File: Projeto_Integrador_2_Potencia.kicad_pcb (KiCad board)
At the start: 2 copper layers, 114 x 59.4 mm, 17 parts, among them J10 Borne_CMD_Interface, J2 Vi 24V, J3 Vo 48V, J4 INA219_01x02_Socket_3.5mm, J5 INA219_01x06_Socket_2.55mm, J7 Display_01x04_Socket, J9 PWM_Connector, Q1 IRF740, U1 ESP32-DEVKIT-V1

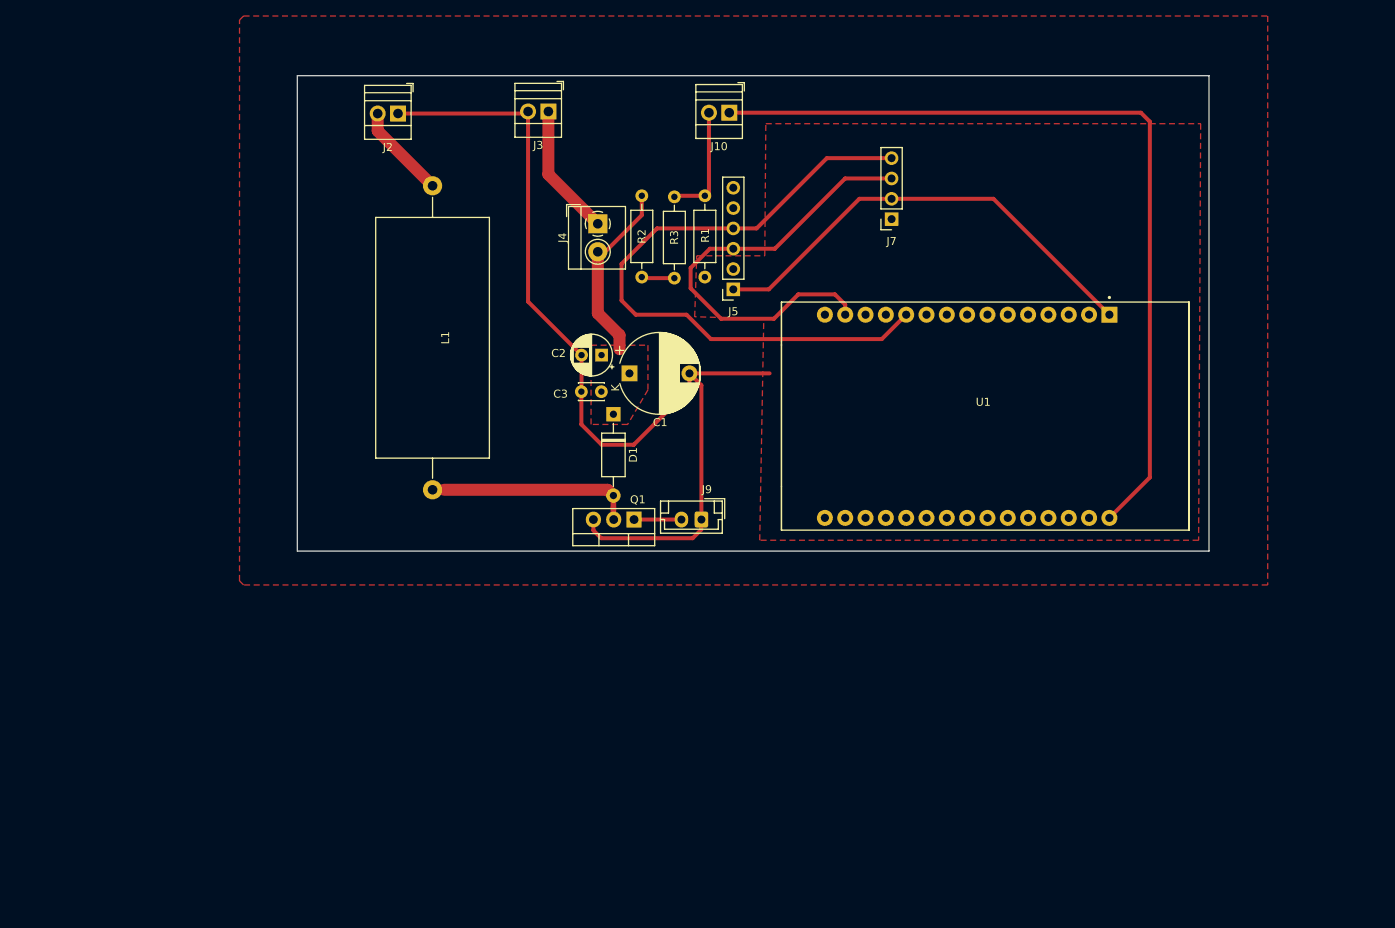
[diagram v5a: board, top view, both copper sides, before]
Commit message: Adição de recuo nas bordas do layout
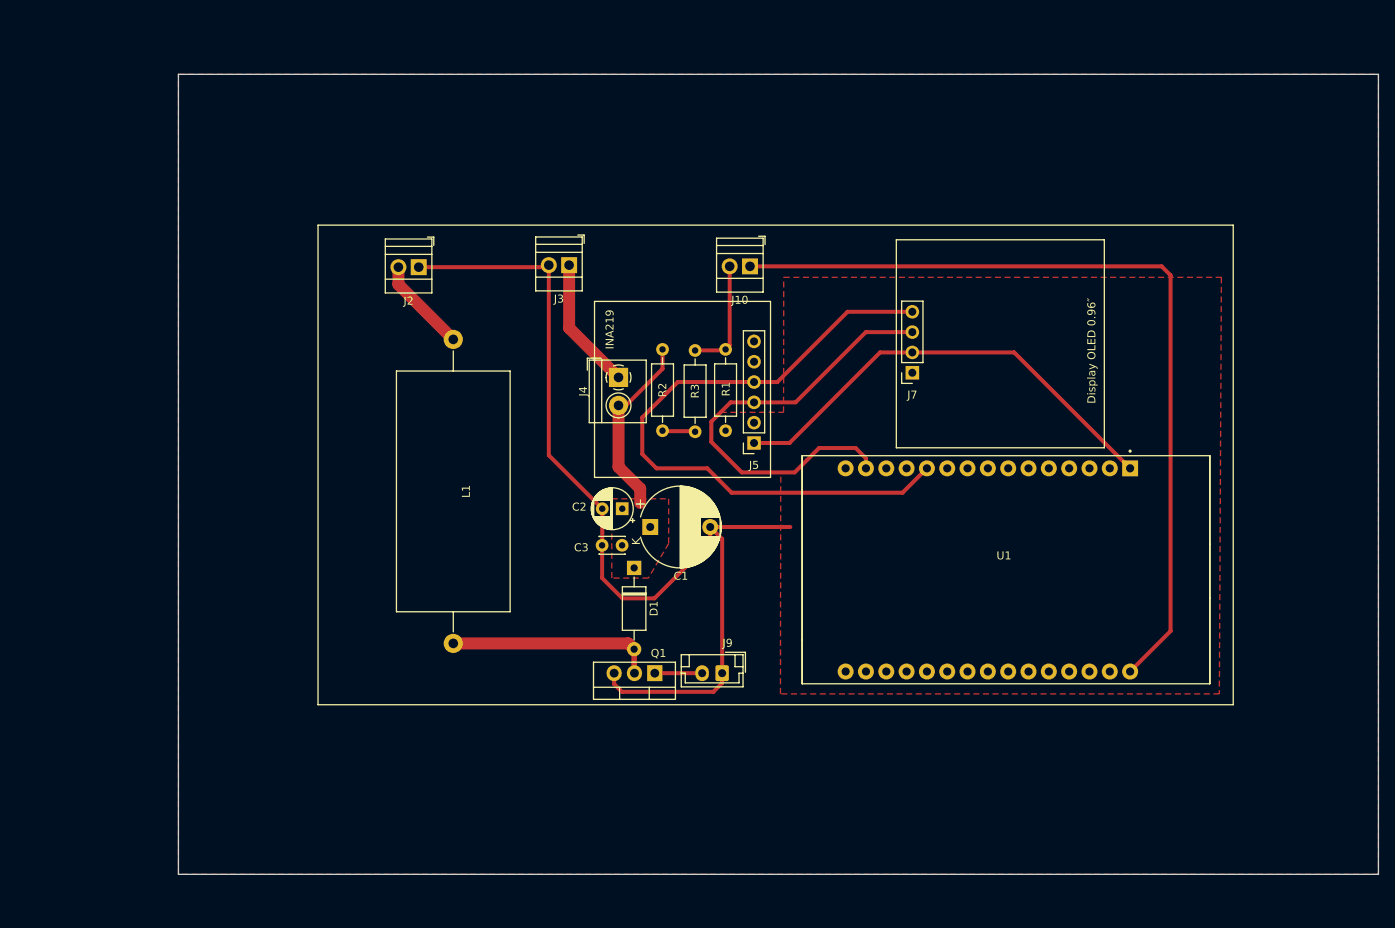
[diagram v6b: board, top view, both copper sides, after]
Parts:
- moved J10 19.4 mm to (135.9, 69.9)
- moved J2 19.4 mm to (94.5, 70.0)
- moved R1 19.4 mm to (132.9, 80.3)
- moved D1 19.4 mm to (121.5, 107.6)
- moved J4 19.4 mm to (119.5, 83.8)
- moved L1 19.4 mm to (98.9, 79.0)
- moved R2 19.4 mm to (125.0, 80.3)
- moved R3 19.4 mm to (129.1, 90.6)
- moved J3 19.4 mm to (113.3, 69.8)
- moved J7 19.4 mm to (156.2, 83.2)
- moved C3 19.4 mm to (120.0, 104.8)
- moved J5 19.4 mm to (136.4, 92.0)
- moved Q1 19.4 mm to (124.0, 120.8)
- moved C1 19.4 mm to (123.5, 102.5)
- moved C2 19.4 mm to (120.0, 100.2)
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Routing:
- net Net-(D1-A): track 26.0 -> 27.4 mm
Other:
- board size 114 x 59.4 mm -> 150 x 100 mm

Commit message: Mudanças após primeira manufatura
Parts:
- added Q2: 47N60, Package_TO_SOT_THT:TO-247-3_Vertical, F.Cu at (112.0, 137.3)
- C1: footprint Capacitor_THT:CP_Radial_D10.0mm_P7.50mm -> Capacitor_THT:CP_Radial_D16.0mm_P7.50mm
- C2: footprint Capacitor_THT:CP_Radial_D5.0mm_P2.50mm -> Capacitor_THT:CP_Radial_D8.0mm_P5.00mm
- D1: value ~ -> Diodo Schottky; footprint Diode_THT:D_A-405_P10.16mm_Horizontal -> Diode_THT:D_DO-27_P15.24mm_Horizontal
- J10, J2, J3: footprint TerminalBlock:TerminalBlock_Xinya_XY308-2.54-2P_1x02_P2.54mm_Horizontal -> TerminalBlock:TerminalBlock_bornier-2_P5.08mm
- L1: footprint Inductor_THT:L_Axial_L29.9mm_D14.0mm_P38.00mm_Horizontal_Vishay_IHA-105 -> Integrador_2:Indutor_Integrador_2
- moved L1 25.0 mm to (77.7, 92.5), turned to 180 degrees
- moved J9 16.8 mm to (135.6, 137.3)
- moved Q1 16.8 mm to (109.1, 128.5)
- moved J10 15.3 mm to (146.1, 58.4)
- moved J3 14.4 mm to (122.2, 58.4)
- moved J2 11.6 mm to (94.3, 58.4)
- moved U1 10.3 mm to (173.5, 116.6)
- moved C1 6.79 mm to (129.9, 104.6)
- moved C3 6.45 mm to (115.3, 109.2)
- moved D1 6.25 mm to (122.2, 113.8)
- moved R3 5.30 mm to (131.7, 86.0)
- moved J4 5.24 mm to (122.2, 79.3)
- moved R1 5.18 mm to (135.5, 75.8)
- moved R2 5.18 mm to (127.6, 75.8)
- moved J5 5.18 mm to (139.1, 87.5)
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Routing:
- net GND: track 123.5 -> 206.3 mm
- net 3V3: track 57.6 -> 87.3 mm
- net pwm: track 5.92 -> 31.8 mm
- net Net-(D1-A): track 27.4 -> 52.6 mm
- net I2C_Sda: track 82.6 -> 61.2 mm
- net 8V: track 104.7 -> 116.8 mm
- net 5.2V_feedback: track 14.5 -> 23.5 mm
- net INA_Vin+: track 16.6 -> 20.9 mm
- net Net-(J2-Pin_2): track 11.9 -> 13.0 mm
- net I2C_Scl: track 56.2 -> 55.3 mm
- net INA_Vin-: track 23.1 -> 23.9 mm
- added copper zone on B.Cu, net (none)
- added copper zone on B.Cu, net GND
- added copper zone on B.Cu, net INA_Vin-
- removed copper zone on F.Cu, net (none)
- removed copper zone on F.Cu, net GND
- removed copper zone on F.Cu, net INA_Vin-
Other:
- board size 150 x 100 mm -> 149.7 x 95.2 mm

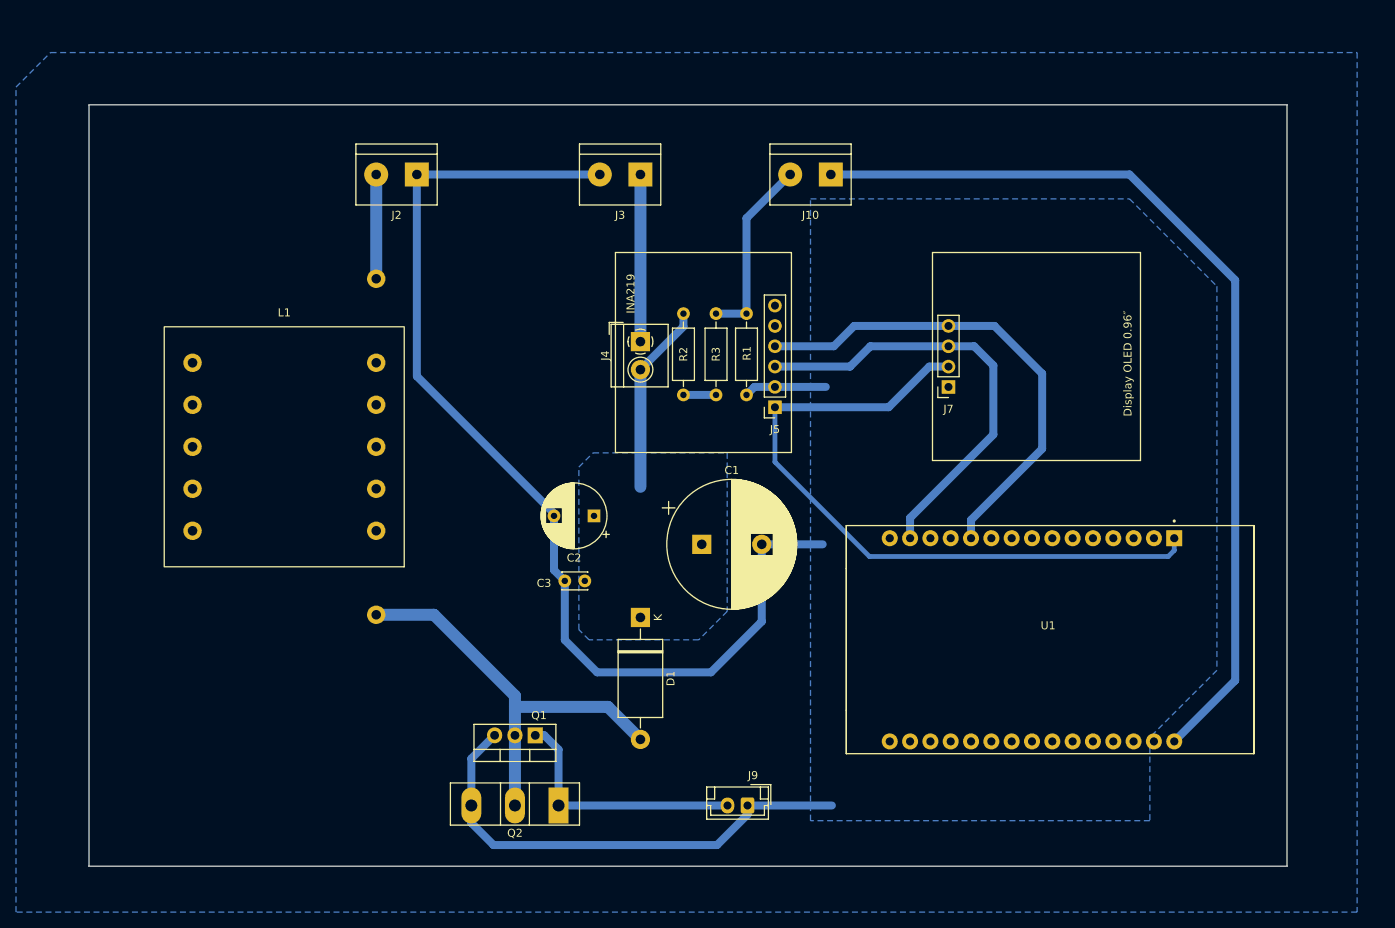
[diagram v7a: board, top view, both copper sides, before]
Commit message: Alargamento de trilhas e pads
Correção do valor do capacitor cerâmico
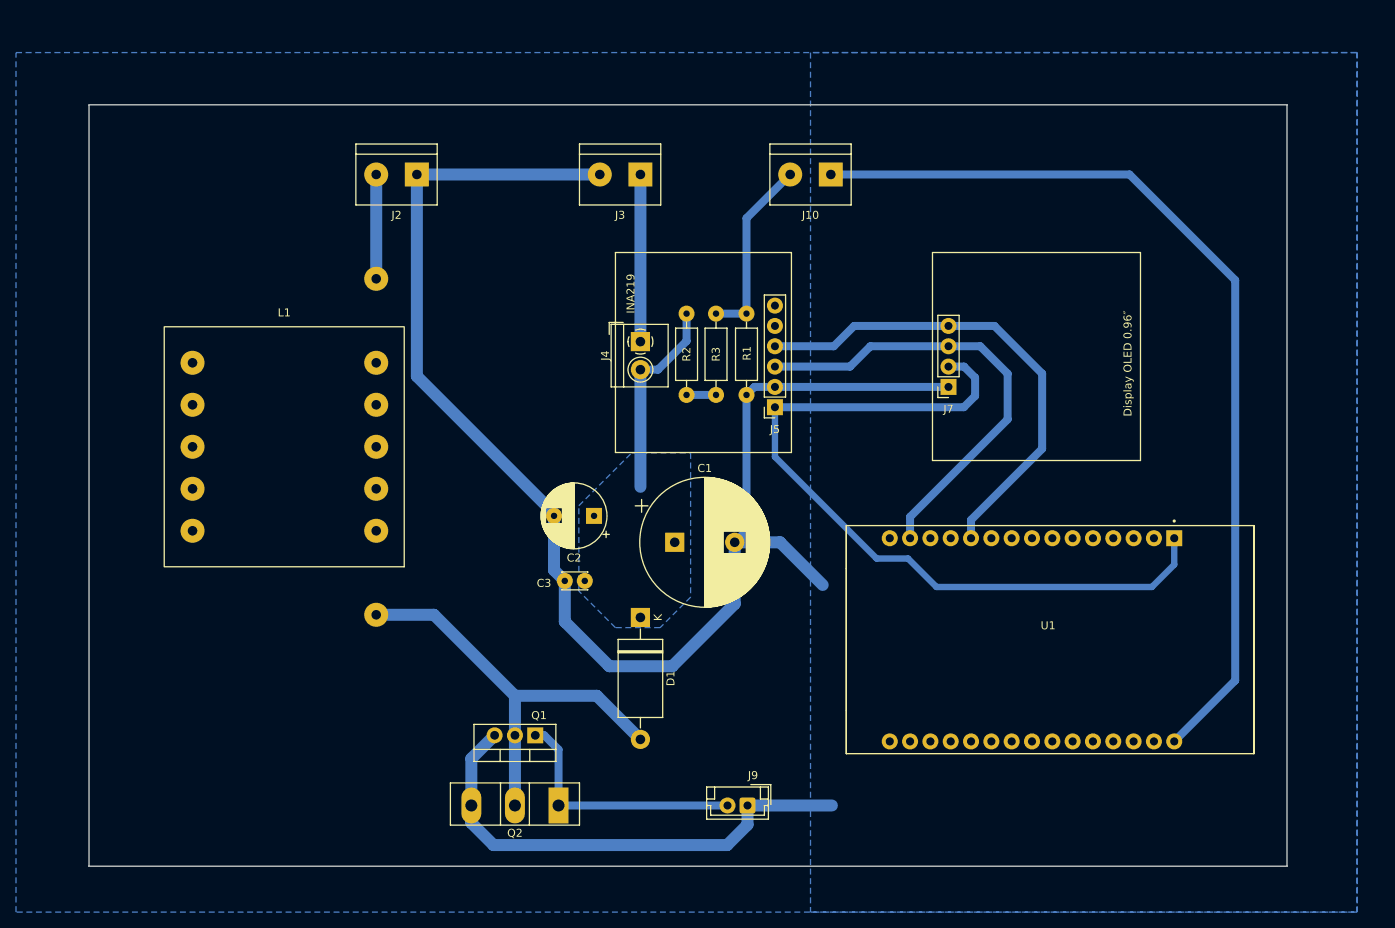
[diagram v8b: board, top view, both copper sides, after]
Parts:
- moved C1 3.39 mm to (126.5, 104.4)
- moved R2 0.39 mm to (128.0, 75.8)
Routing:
- net GND: track 206.3 -> 240.6 mm
- net 3V3: track 87.3 -> 99.1 mm
- net I2C_Scl: track 55.3 -> 57.2 mm
- net INA_Vin-: track 23.9 -> 25.3 mm
- net Net-(D1-A): track 52.6 -> 53.2 mm
